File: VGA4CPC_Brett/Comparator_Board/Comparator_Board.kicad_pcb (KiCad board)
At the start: 2 copper layers, 25.4 x 19.7 mm, 18 parts, among them J1 INPUT, J2 OUTPUT, U1 TLV3232, U2 TLV3232, U3 TLV3232

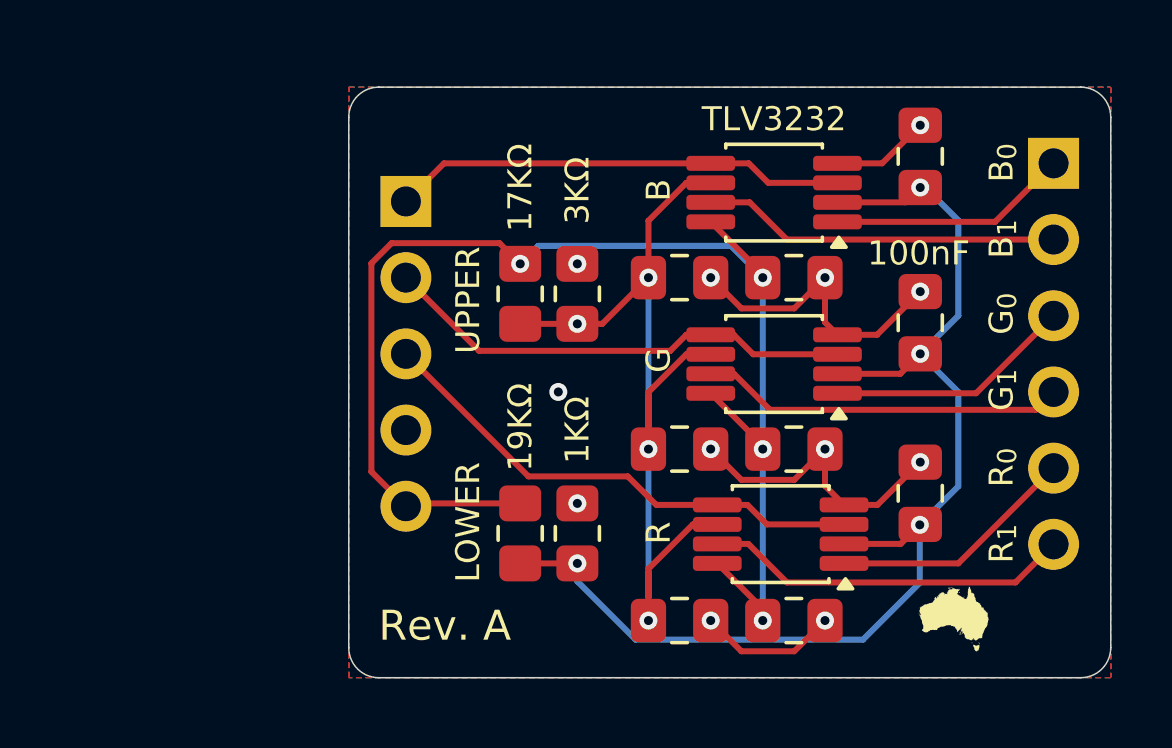
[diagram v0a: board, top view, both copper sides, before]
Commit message: Widened the PCB
Made more room on the PCB in case we want to change it and not have to change the footprint on the main board.
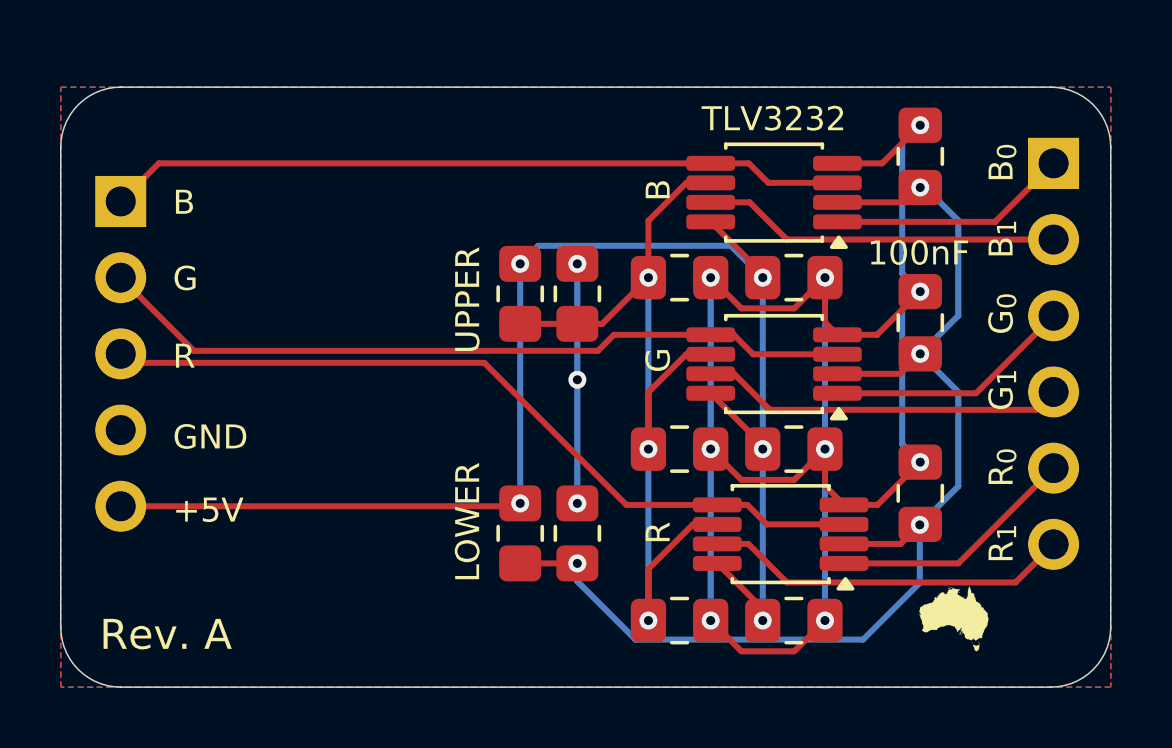
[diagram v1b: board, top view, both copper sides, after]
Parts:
- moved J1 9.50 mm to (77.3, 58.3)
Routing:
- net GND: track 28.0 -> 71.0 mm
- net /CPC_B: track 15.2 -> 24.7 mm
- net /CPC_R: track 17.0 -> 26.5 mm
- net /CPC_G: track 15.9 -> 25.4 mm
- net +5V: track 45.8 -> 49.2 mm, vias 4 -> 5
- net /UPPER: vias 4 -> 3
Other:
- board size 25.4 x 19.7 mm -> 35 x 20 mm
- board text added: "RGB Comparator Brett Hallen, May 2026"
- board text removed: "CPC_B"
- board text removed: "CPC_G"
- board text removed: "CPC_R"
